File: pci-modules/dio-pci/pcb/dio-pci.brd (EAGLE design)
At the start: 167.6 x 111.2 mm, 124 parts, among them Q1 BSH103, Q2 BSH103, U1 4901, U2 7933, U3 ADN4663, U4 ADN4663, U5 ADN4664, U6 PDS1, U7 4901

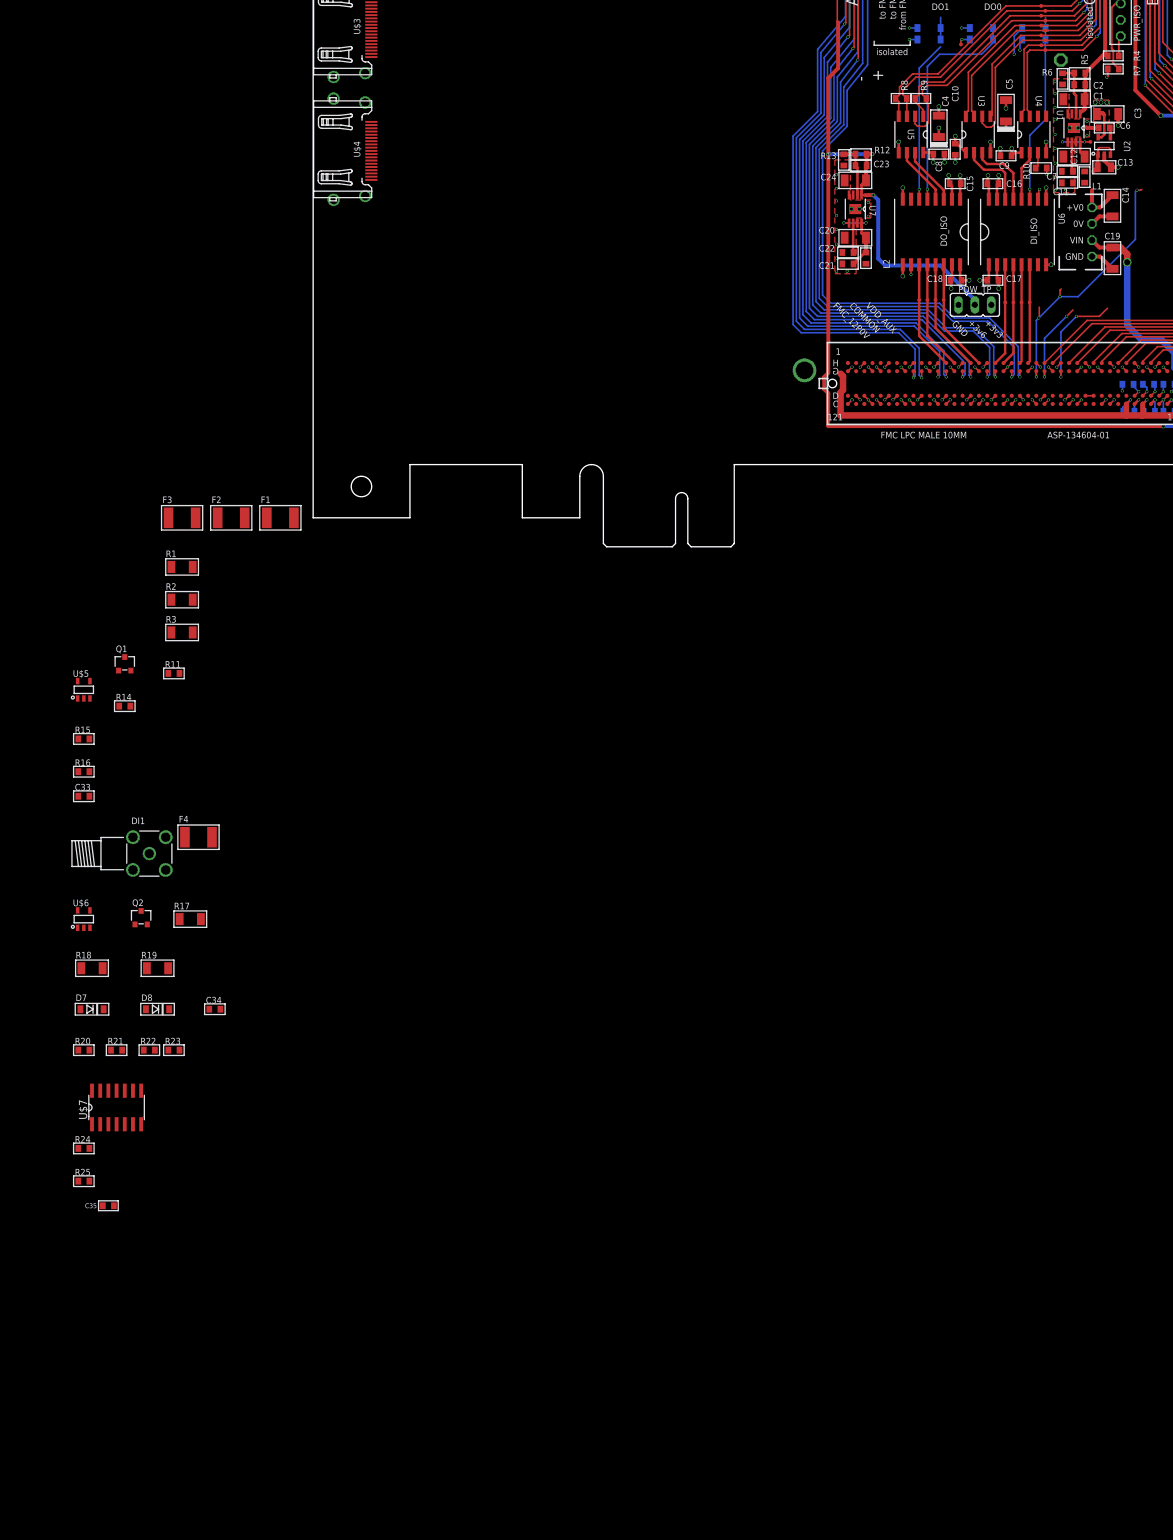
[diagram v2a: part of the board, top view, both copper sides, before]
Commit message: Designed protection network for dio-pci card
- TTL, LVTTL, CMOS logic level compatible
- Resistant to incorrect logic levels and low impedance DC or AC sources
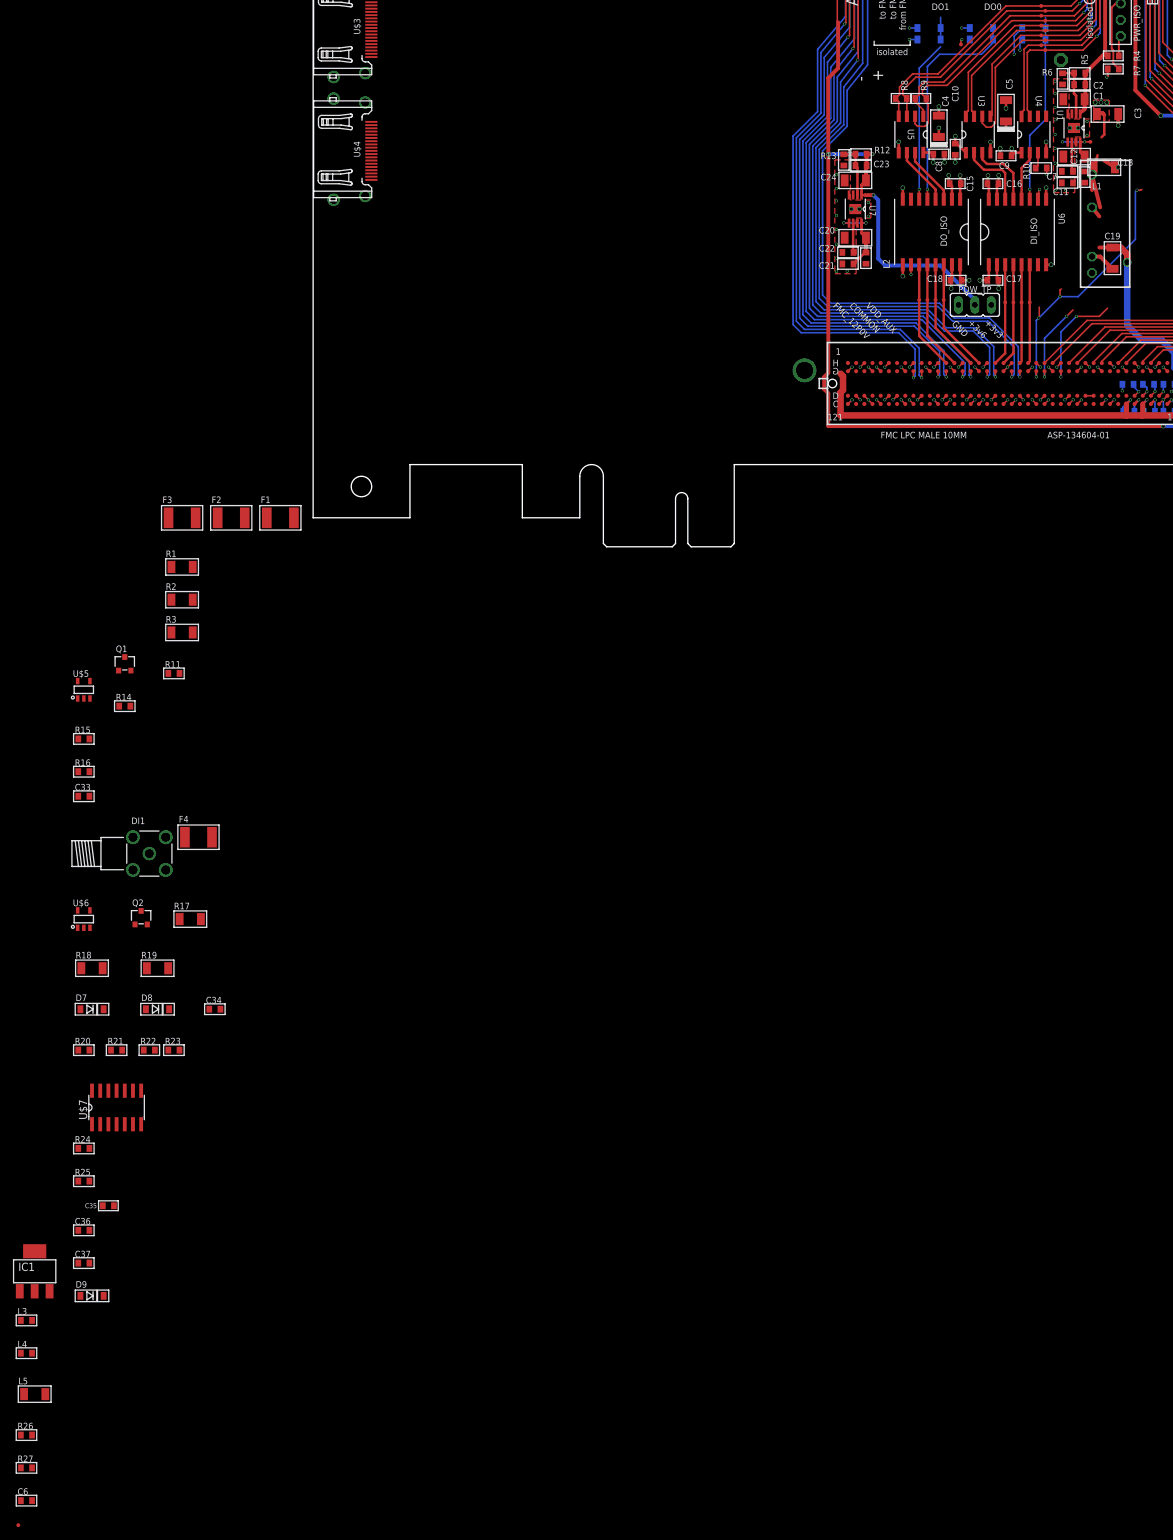
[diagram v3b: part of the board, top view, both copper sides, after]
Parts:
- removed C14: 10uF, jonnew:1206
- removed U2: 7933, jonnew:SOT-23-5
- added C36, C37: 0.1uF, jonnew:0603
- added D9: KDZ4.3B, jonnew:SOD123
- added IC1: AZ1117CH-3.3, jonnew:SOT223
- added L3, L4: MPZ1608, jonnew:0603
- added L5: 82103C, jonnew:1206
- added R26, R27: 2.2k, jonnew:0603
- added TP8: +5V0, jonnew:TP06R
- C13: value 1.0uF -> 10uF; device RHD2000_eval_board:0805 -> jonnew:1206
- C6: value 10nF -> 0.1uF; device RHD2000_eval_board:0603 -> jonnew:0603
- U6: value PDS1 -> MEV3S1209SC; device jonnew:PDS1 -> jonnew:MEV3
- moved C6 270.6 mm to (-44.5, -152.4), turned to 0 degrees
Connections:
- removed net N$97: C6.1, U2.4
- new net +9V0_ISO: L1.1, L2.1, L3.1, R26.2, R27.2, U6.P4
- new net N$21: C13.1, IC1.4, L3.2
- new net N$22: IC1.3, L4.1
- new net N$23: L5.2, U6.P1
- net +3V3_ISO: now also C36.1, C37.1, L4.2; no longer D3.C, D5.C, U2.5
- net +5V0: no longer C13.1, C14.1, L1.1, L2.1, U2.1, U2.3, U6.P4
- net 12V_FPGA: now also L5.1; no longer U6.P2
- net GND: now also U6.P2; no longer U6.P1
- net GND_ISO: now also C36.2, C37.2, C6.1, D9.A, IC1.1; no longer C14.2, C6.2, U2.2
- net V_PROTECT: now also C6.2, D3.C, D5.C, D9.C, R26.1, R27.1, TP8.TP
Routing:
- net +5V0: track 18.5 -> 5.01 mm
- net +9V0_ISO: track 0.00 -> 7.62 mm
- net GND_ISO: track 42.4 -> 37.6 mm
- net +3V3_ISO: track 31.7 -> 28.7 mm, vias 14 -> 13
- net N$21: track 0.00 -> 2.62 mm
- net 12V_FPGA: track 115.7 -> 114.1 mm
- net N$97: track 1.50 -> 0.00 mm
- net V_PROTECT: track 1.80 -> 3.05 mm, vias 1 -> 2

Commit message: Added some design ideas to dio-pci README.
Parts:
- removed U$3, U$4: HDMI, jonnew:HDMI_A
- L5: device jonnew:1206 -> jonnew:1210
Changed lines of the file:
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@@
 </element>
 <element name="U$2" library="jonnew" package="PCI-ADDIN_STD-H_HALF-L" value="PCI-MECH_STD-H_HALF-W" x="0" y="0"/>
-<element name="U$3" library="jonnew" package="HDMI_A" value="HDMI" x="5.08" y="76.2" rot="R270"/>
-<element name="U$4" library="jonnew" package="HDMI_A" value="HDMI" x="5.08" y="57.15" rot="R270"/>
 <element name="F1" library="jonnew" package="1812" value="C014F-2" x="-5.08" y="0"/>
 <element name="F2" library="jonnew" package="1812" value="C014F-2" x="-12.7" y="0"/>
@@
 <element name="L3" library="jonnew" package="0603" value="MPZ1608" x="-44.45" y="-124.46"/>
 <element name="L4" library="jonnew" package="0603" value="MPZ1608" x="-44.45" y="-129.54"/>
-<element name="L5" library="jonnew" package="1206" value=" 82103C" x="-43.18" y="-135.89"/>
+<element name="L5" library="jonnew" package="1210" value=" 82103C" x="-43.18" y="-135.89"/>
 <element name="R26" library="jonnew" package="0603" value="2.2k" x="-44.45" y="-142.24">
 <attribute name="MN" value="Panasonic" x="-44.45" y="-142.24" size="1.778" layer="27" display="off"/>
@@
 <wire x1="125.222" y1="41.91" x2="123.952" y2="41.91" width="1.016" layer="1"/>
 <contactref element="L5" pad="1"/>
-<wire x1="81.788" y1="15.875" x2="-44.831" y2="-135.89" width="0" layer="19" extent="1-1"/>
+<wire x1="81.788" y1="15.875" x2="-44.577" y2="-135.89" width="0" layer="19" extent="1-1"/>
 </signal>
 <signal name="N$5">
@@
 <contactref element="U6" pad="P1"/>
 <contactref element="L5" pad="2"/>
-<wire x1="120.777" y1="37.973" x2="-41.529" y2="-135.89" width="0" layer="19" extent="1-1"/>
+<wire x1="120.777" y1="37.973" x2="-41.783" y2="-135.89" width="0" layer="19" extent="1-1"/>
 </signal>
 <signal name="+9V0_ISO">
